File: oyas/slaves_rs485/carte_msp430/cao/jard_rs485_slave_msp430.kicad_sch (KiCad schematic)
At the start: 60 parts, among them J1 POWER, J5 Prog MSP, U1 BPC_Alim3_3V, U1 MAX485E, U2 MSP430F1232IDW, Y1 8MHz

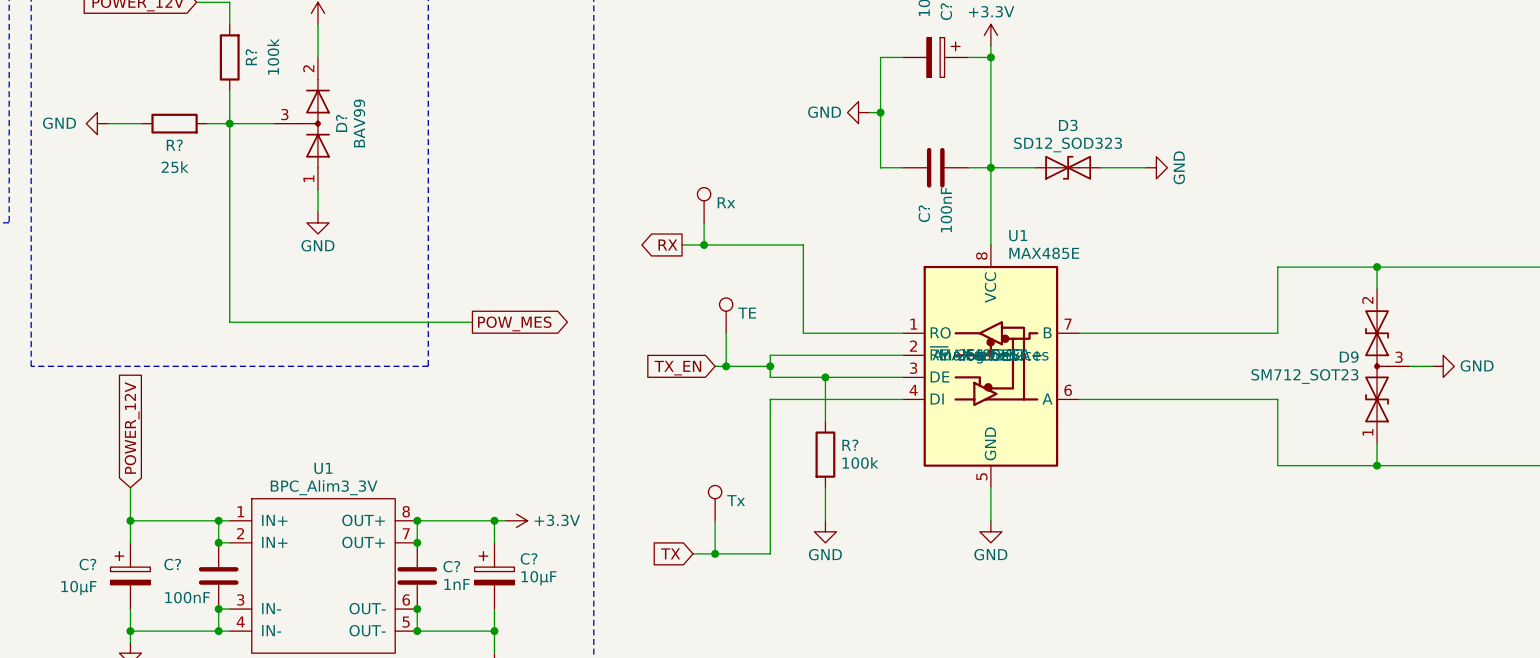
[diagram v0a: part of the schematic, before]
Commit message: Modif MAX485 -> MAX3485 (3.3V)
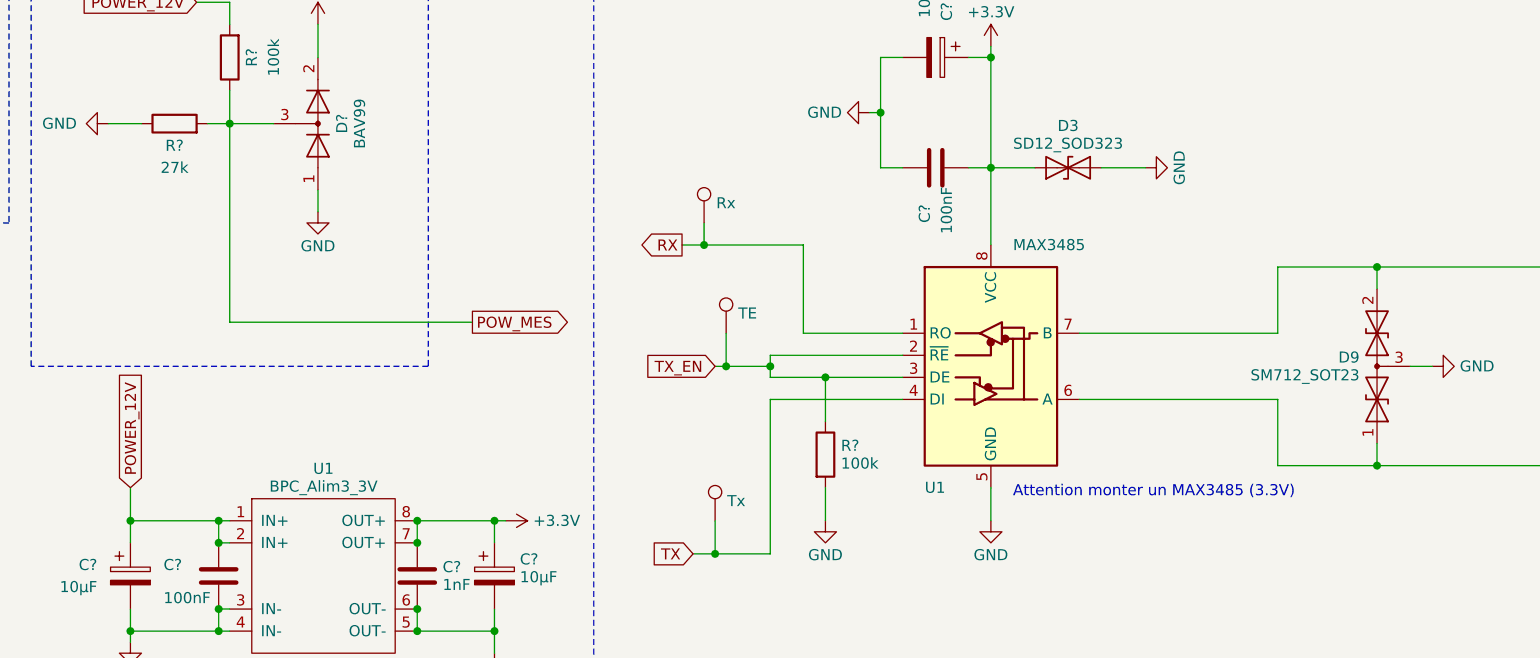
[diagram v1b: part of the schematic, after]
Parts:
- R?: value 25k -> 27k
- U1: value MAX485E -> MAX3485
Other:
- note added: "Attention monter un MAX3485 (3.3V)"
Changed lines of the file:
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@@
     (effects (font (size 1.27 1.27)) (justify left bottom))
   )
+  (text "Attention monter un MAX3485 (3.3V)" (at 194.31 76.2 0)
+    (effects (font (size 1.27 1.27)) (justify left bottom))
+  )
   (global_label "LED" (shape output) (at 160.02 173.99 0) (fields_autoplaced)
     (effects (font (size 1.27 1.27)) (justify left))
@@
   )
   (symbol (lib_id "bpc:BPC_MAX485E") (at 191.77 59.69 0) (unit 1)
-    (in_bom yes) (on_board yes) (dnp no) (fields_autoplaced)
-    (property "Reference" "U1" (at 193.7259 45.95 0)
+    (in_bom yes) (on_board yes) (dnp no)
+    (property "Reference" "U1" (at 184.15 74.93 0)
       (effects (font (size 1.27 1.27)) (justify left))
     )
-    (property "Value" "MAX485E" (at 193.7259 47.998 0)
+    (property "Value" "MAX3485" (at 194.31 46.99 0)
       (effects (font (size 1.27 1.27)) (justify left))
     )
@@
       (effects (font (size 1.27 1.27)) hide)
     )
-    (property "Fabricant" "Analog Devices" (at 191.77 59.69 0)
-      (effects (font (size 1.27 1.27)))
+    (property "Fabricant" "Analog Devices" (at 193.7259 41.854 0)
+      (effects (font (size 1.27 1.27)) (justify left) hide)
     )
-    (property "Fournisseur" "Farnell" (at 191.77 59.69 0)
-      (effects (font (size 1.27 1.27)))
+    (property "Fournisseur" "Farnell" (at 193.7259 43.902 0)
+      (effects (font (size 1.27 1.27)) (justify left) hide)
     )
-    (property "RefFabricant" "MAX485ESA+" (at 191.77 59.69 0)
-      (effects (font (size 1.27 1.27)))
+    (property "RefFabricant" "MAX485ESA+" (at 193.7259 45.95 0)
+      (effects (font (size 1.27 1.27)) (justify left) hide)
     )
-    (property "RefFournisseur" "2519382" (at 191.77 59.69 0)
-      (effects (font (size 1.27 1.27)))
+    (property "RefFournisseur" "2519382" (at 193.7259 47.998 0)
+      (effects (font (size 1.27 1.27)) (justify left) hide)
     )
     (pin "1")
@@
       (effects (font (size 1.27 1.27)))
     )
-    (property "Value" "25k" (at 97.79 38.1 90)
+    (property "Value" "27k" (at 97.79 38.1 90)
       (effects (font (size 1.27 1.27)))
     )
